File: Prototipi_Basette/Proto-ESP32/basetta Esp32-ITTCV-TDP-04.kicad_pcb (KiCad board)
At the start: 2 copper layers, 76.6 x 67.5 mm, 35 parts, among them J1 Conn_01x19, J2 Conn_01x19, J3 Conn_01x19, J4 Conn_01x19, J5 Screw_Terminal_01x02, J6 Conn_01x05, J7 Conn_01x02, J8 Conn_01x05, J9 Conn_01x05, Q1 BC557, Q2 BC547, Q3 BC547, Q4 BC547, Q5 IRF9540N, SW1 RESET, SW2 SET, U3 4013

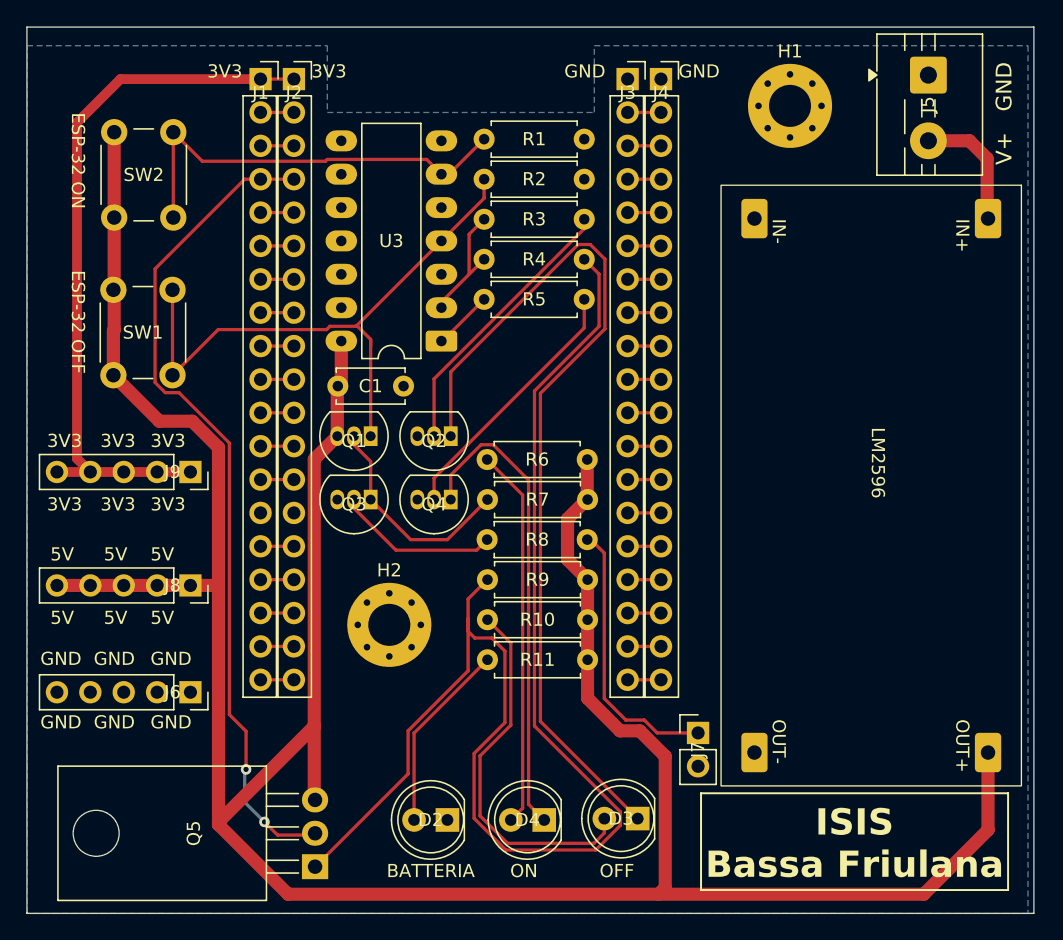
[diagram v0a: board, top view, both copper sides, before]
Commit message: Add ITTCV-TDP-04 ESP32 board variant
Add new KiCad project files for the basetta Esp32-ITTCV-TDP-04 variant (basetta Esp32-ITTCV-TDP-04.kicad_pcb, .kicad_prl, .kicad_sch). Also update the main basetta Esp32 files (basetta Esp32.kicad_pcb, .kicad_prl, basetta Esp32.kicad_pro) to reflect recent changes. The new PCB file contains the full layout and footprints for the variant; .prl and .sch provide the panel/run and schematic support.
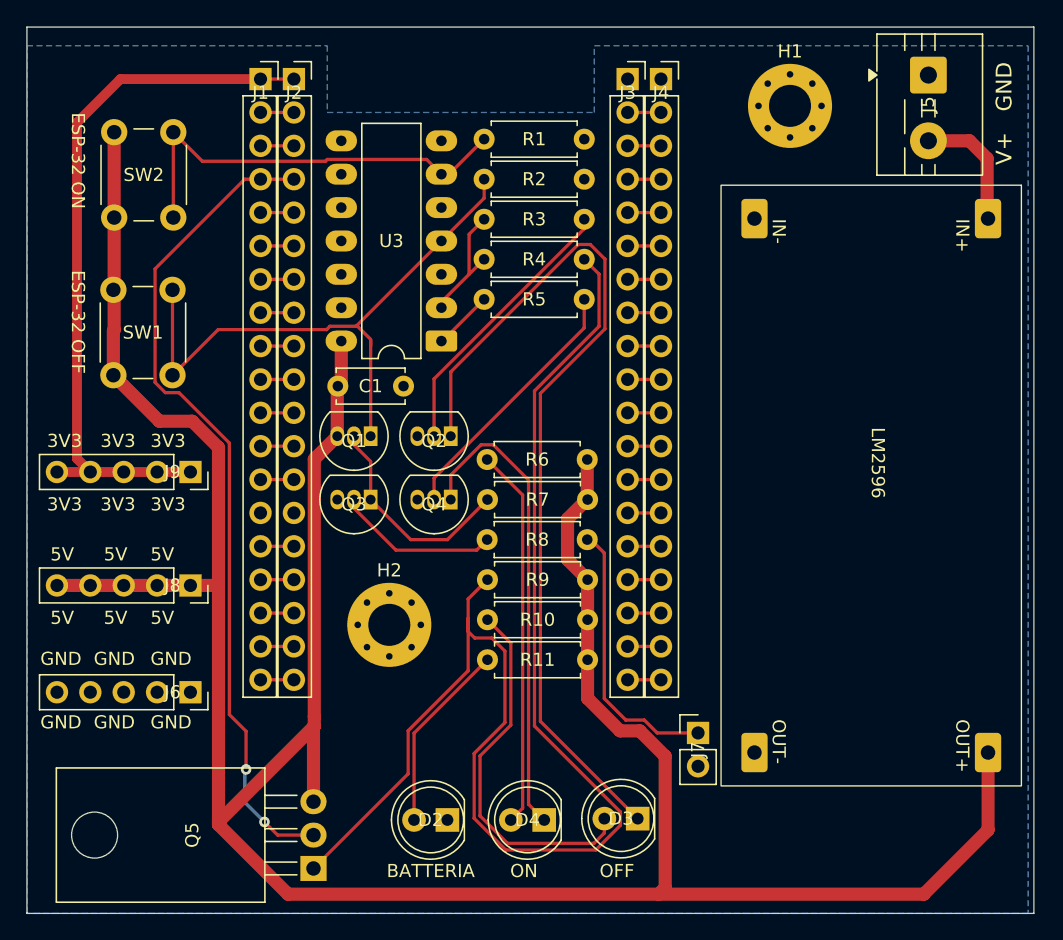
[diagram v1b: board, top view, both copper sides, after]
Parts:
- moved Q5 0.18 mm to (143.7, 121.0)
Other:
- board text removed: "3V3"
- board text removed: "GND"
- board text removed: "ISIS Bassa Friulana"
